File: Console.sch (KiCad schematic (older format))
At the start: 15 parts, among them CON1 CONSOLE, U16 FT230XS

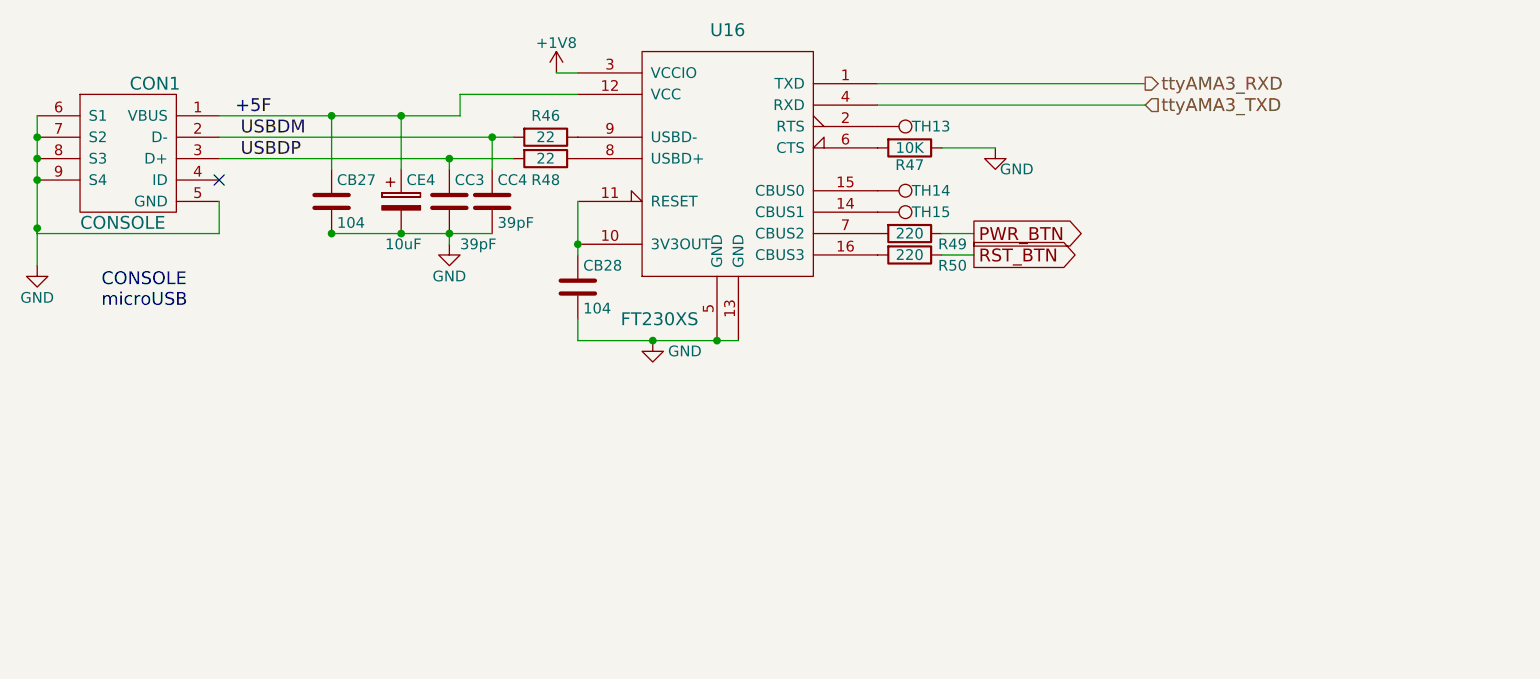
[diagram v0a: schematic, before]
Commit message: Deleted unnecessary files and splitting schmatics.
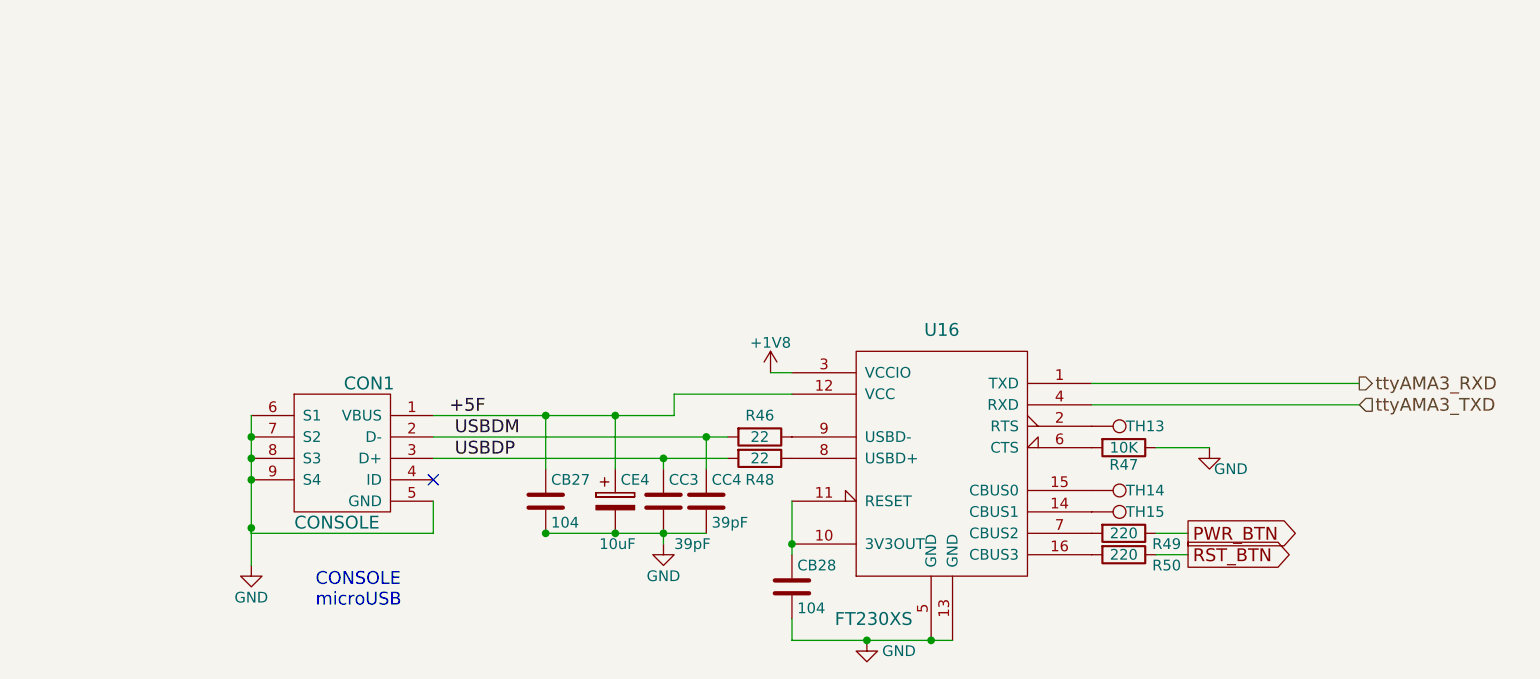
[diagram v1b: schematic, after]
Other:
- moved on the sheet: CB27, CB28, CC3, CC4, CE4, CON1, R46, R47, R48, R49, R50, TH13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
